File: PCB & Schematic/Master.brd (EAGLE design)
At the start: 80 x 53.3 mm, 25 parts, among them M1 ARDUINO_R3_ICSP_NODIM, X1 MAB5SH, X2 MAB5SH

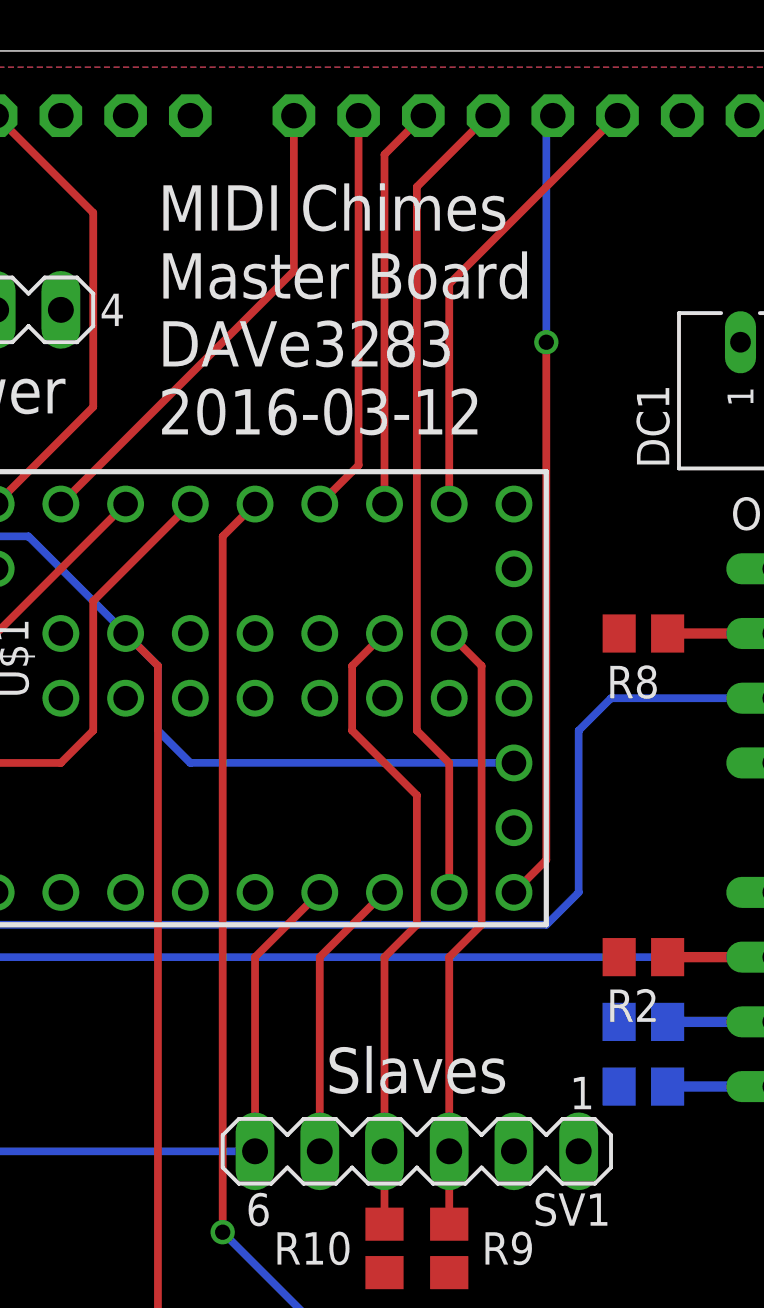
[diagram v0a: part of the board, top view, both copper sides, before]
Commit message: Move LCD DC Pin to a physical CS pin on the Teensy.
I failed to notice the library won't support the display if both
CS and DC pins aren't on hardware CS pins. D'oh!
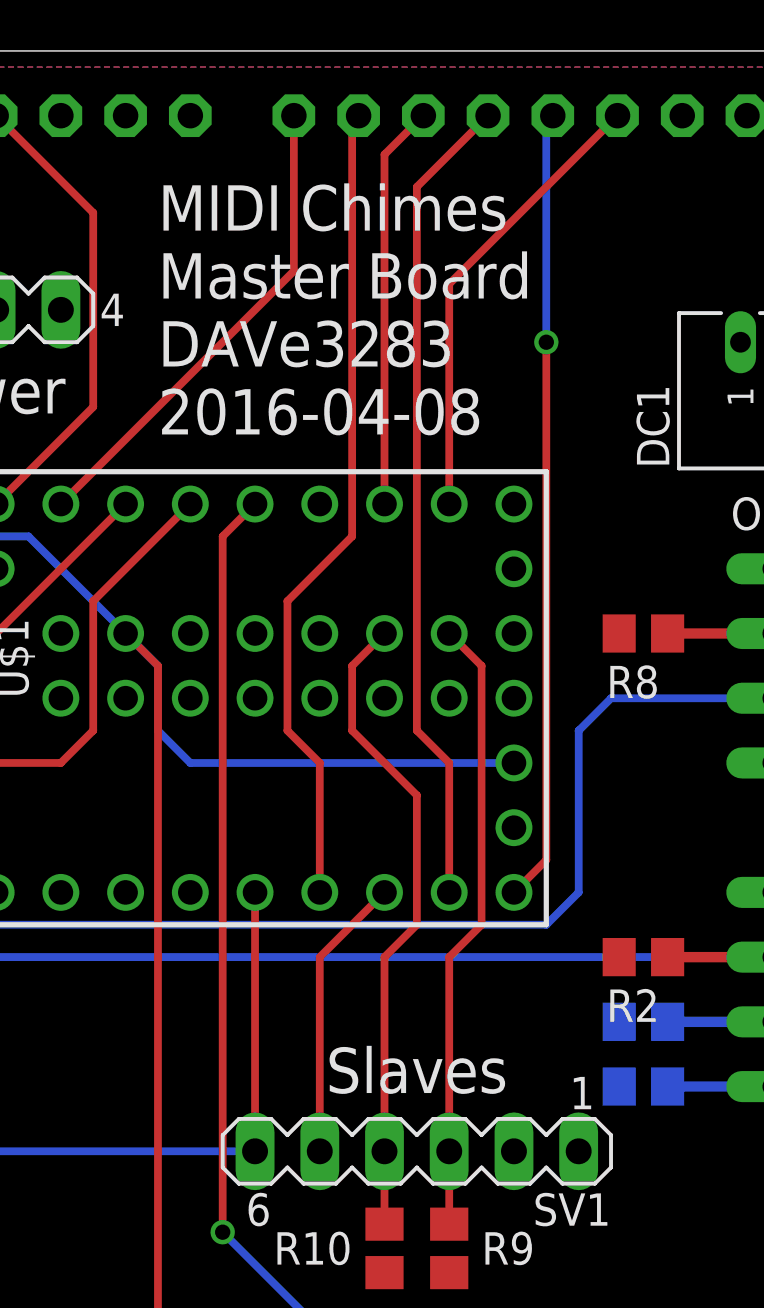
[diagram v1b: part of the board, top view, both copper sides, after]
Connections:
- net LCD_DC: now also U$1.9; no longer U$1.16/A2
- net PS_EN: now also U$1.8; no longer U$1.9
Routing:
- net LCD_DC: track 15.9 -> 32.2 mm
- net PS_EN: track 73.1 -> 72.1 mm
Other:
- board text added: "MIDI Chimes Master Board DAVe3283 2016-04-08"
- board text removed: "MIDI Chimes Master Board DAVe3283 2016-03-12"
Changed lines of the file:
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@@
 Master Board
 DAVe3283
-2016-03-12</text>
+2016-04-08</text>
 <text x="53.34" y="4.445" size="2.54" layer="25" align="center">MIDI
 IN</text>
@@
 <signal name="PS_EN">
 <contactref element="SV1" pad="6"/>
-<contactref element="U$1" pad="9"/>
 <wire x1="4.135" y1="45.41" x2="3.81" y2="45.085" width="0.3048" layer="1"/>
 <wire x1="3.81" y1="45.085" x2="3.175" y2="45.085" width="0.3048" layer="1"/>
@@
 <wire x1="3.175" y1="45.085" x2="0.635" y2="42.545" width="0.3048" layer="16"/>
 <wire x1="0.635" y1="42.545" x2="0.635" y2="12.065" width="0.3048" layer="16"/>
-<wire x1="27.94" y1="20.32" x2="25.4" y2="17.78" width="0.3048" layer="1"/>
-<wire x1="25.4" y1="17.78" x2="25.4" y2="10.16" width="0.3048" layer="1"/>
+<contactref element="U$1" pad="8"/>
+<wire x1="25.4" y1="10.16" x2="25.4" y2="20.32" width="0.3048" layer="1"/>
 </signal>
 <signal name="ADDR_LATCH">
@@
 <signal name="LCD_DC">
 <contactref element="M1" pad="D9"/>
-<contactref element="U$1" pad="16/A2"/>
-<wire x1="29.464" y1="50.8" x2="29.464" y2="37.084" width="0.3048" layer="1"/>
-<wire x1="29.464" y1="37.084" x2="27.94" y2="35.56" width="0.3048" layer="1"/>
+<contactref element="U$1" pad="9"/>
+<wire x1="27.94" y1="20.32" x2="27.94" y2="25.4" width="0.3048" layer="1"/>
+<wire x1="27.94" y1="25.4" x2="26.67" y2="26.67" width="0.3048" layer="1"/>
+<wire x1="26.67" y1="26.67" x2="26.67" y2="31.75" width="0.3048" layer="1"/>
+<wire x1="26.67" y1="31.75" x2="29.21" y2="34.29" width="0.3048" layer="1"/>
+<wire x1="29.21" y1="34.29" x2="29.21" y2="50.546" width="0.3048" layer="1"/>
+<wire x1="29.21" y1="50.546" x2="29.464" y2="50.8" width="0.3048" layer="1"/>
 </signal>
 <signal name="LCD_CS">

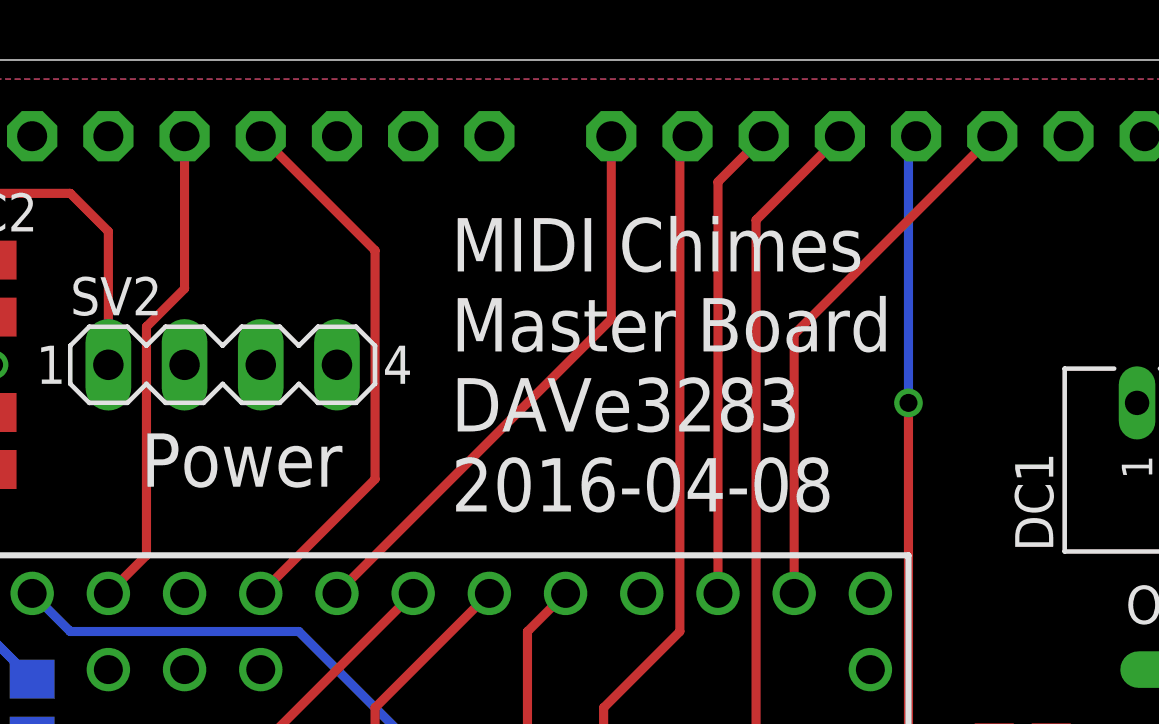
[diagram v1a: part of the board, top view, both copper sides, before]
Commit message: Fix backlight dimming on capacitive TS.
Adafruit's schematic (or my understanding of it?) was wrong, and the
capacitive touchscreen uses digital pin 5 for backlight dimming, not
digital pin 3.

Since most pins are unused, just hooking pins 3 and 5 together works
fine, and requires no other changes. Now the PCB supports either TS.
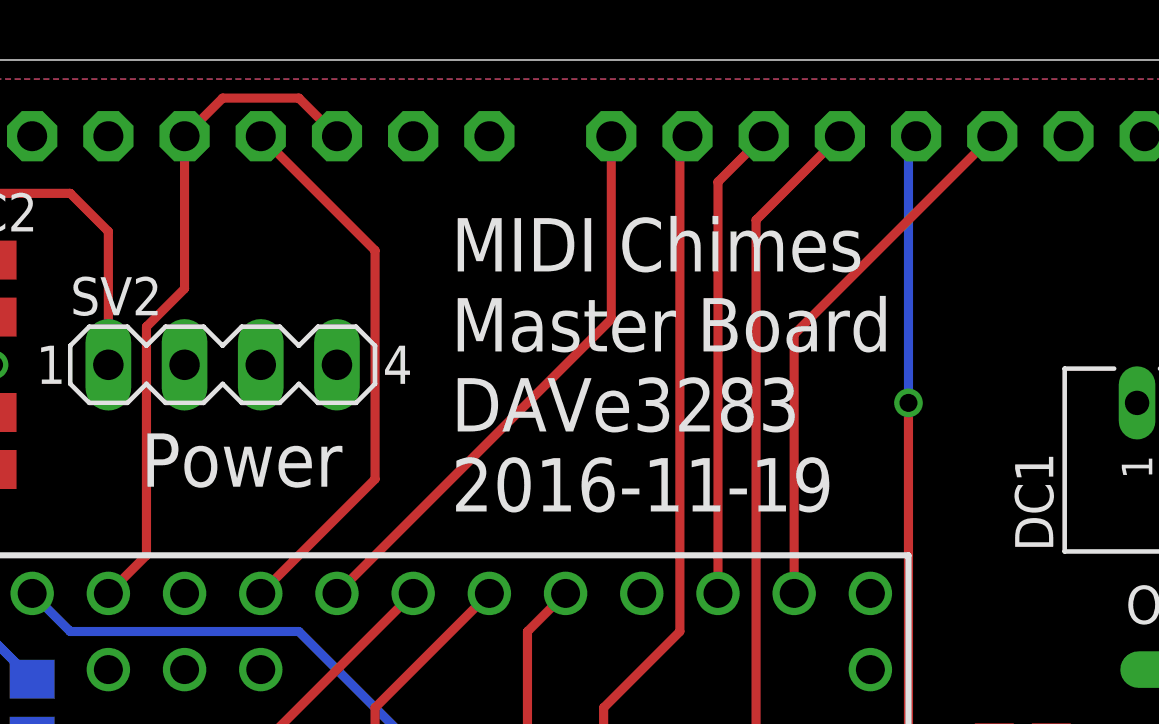
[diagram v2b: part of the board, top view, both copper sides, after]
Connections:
- net LCD_BACKLIGHT: now also M1.D5
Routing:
- net LCD_BACKLIGHT: track 16.3 -> 22.4 mm
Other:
- board text added: "MIDI Chimes Master Board DAVe3283 2016-11-19"
- board text removed: "MIDI Chimes Master Board DAVe3283 2016-04-08"
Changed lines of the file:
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@@
 Master Board
 DAVe3283
-2016-04-08</text>
+2016-11-19</text>
 <text x="53.34" y="4.445" size="2.54" layer="25" align="center">MIDI
 IN</text>
@@
 <wire x1="11.43" y1="44.45" x2="11.43" y2="36.83" width="0.3048" layer="1"/>
 <wire x1="11.43" y1="36.83" x2="10.16" y2="35.56" width="0.3048" layer="1"/>
+<contactref element="M1" pad="D5"/>
+<wire x1="12.7" y1="50.8" x2="13.97" y2="52.07" width="0.3048" layer="1"/>
+<wire x1="13.97" y1="52.07" x2="16.51" y2="52.07" width="0.3048" layer="1"/>
+<wire x1="16.51" y1="52.07" x2="17.78" y2="50.8" width="0.3048" layer="1"/>
 </signal>
 <signal name="TOUCH_SDA">
